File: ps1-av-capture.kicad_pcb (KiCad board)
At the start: 4 copper layers, 100 x 80 mm, 235 parts, among them J1 AV_MULTI_OUT, J2 USB3_B, J3 USB_C_AUDIO, J4 JTAG, J5 UART, SW1 RESET, U1 TVP7002PZP, U10 TLV75733PDBVR, U11 TLV75533PDBVR, U12 PCM2903CDBR, U2 CYUSB3014-BZXI, U3 24LC1025-I/SN, U4 24LC1025-I/SN, U5 TPS563201DDCR, U6 TPS563201DDCR, U7 TPS563201DDCR, U8 TLV75519PDBVR, U9 TLV75519PDBVR, X1 27MHz, Y1 19.2MHz, Y2 12MHz

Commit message: J1: JST PHD 2x7 latching header for a multi-AV pigtail, hand-soldered
Signals paired with grounds in each column, DNP in the JLC assembly.
Pigtail pinout and build steps in docs/design.md, hand-built items in docs/parts.md.
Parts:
- J1: value AV_MULTI_OUT -> AV_PIGTAIL; footprint Connector_PinHeader_2.54mm:PinHeader_1x13_P2.54mm_Vertical -> Connector_JST:JST_PHD_B14B-PHDSS_2x07_P2.00mm_Vertical
- moved J1 2.00 mm to (106.0, 112.0), turned to -90 degrees
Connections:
- J1 pad 1: VIN_G -> VIN_R
- J1 pad 11: AIN_R -> AIN_L
- J1 pad 13: GND -> AIN_R
- J1 pad 2: VIN_R -> GND
- J1 pad 3: unconnected-(J1-Pin_3-Pad3) -> VIN_G
- J1 pad 4: VIN_B -> GND
- J1 pad 5: GND -> VIN_B
- J1 pad 6: unconnected-(J1-Pin_6-Pad6) -> GND
- J1 pad 7: VIN_CVBS -> VIN_Y
- J1 pad 8: VIN_Y -> GND
- J1 pad 9: AIN_L -> VIN_CVBS

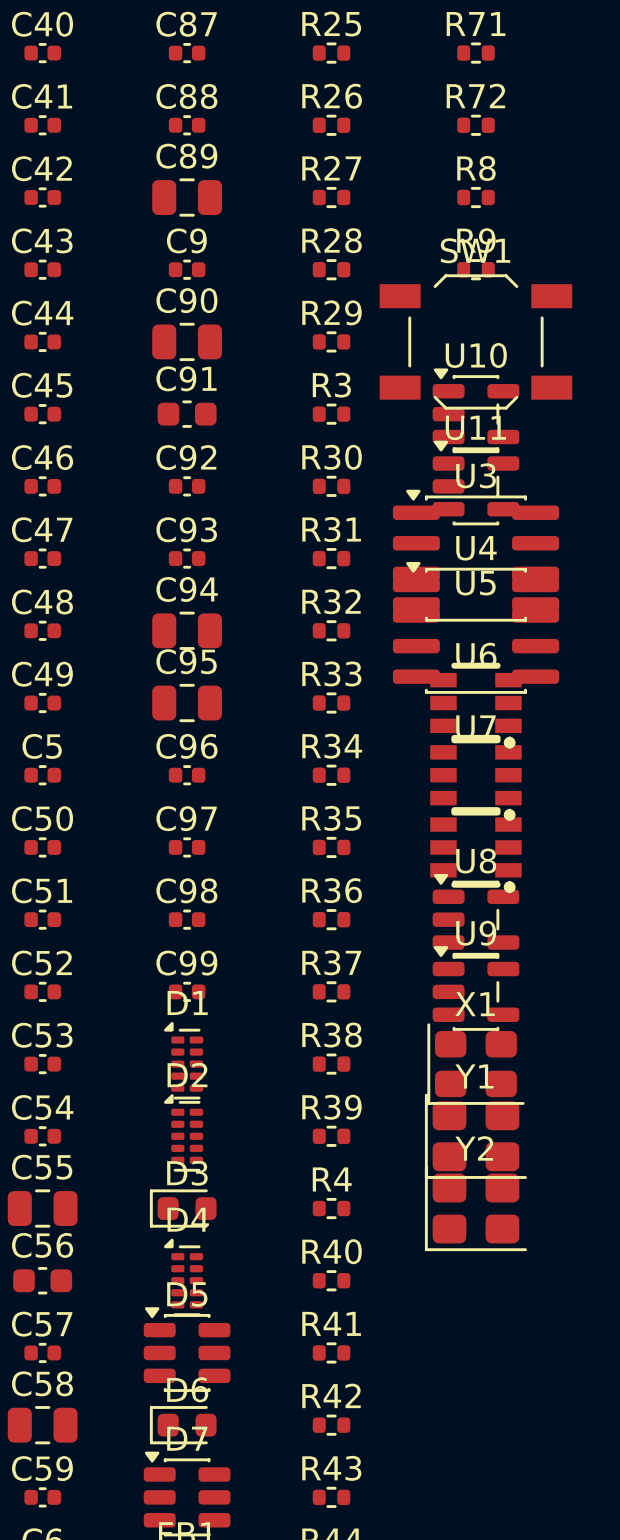
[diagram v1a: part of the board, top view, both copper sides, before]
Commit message: Status LED: common-anode RGB on FX3 GPIO50-52, firmware state map
XL-1615RGBC-RF (C965840) replaces the GPIO57 debug LED. Its LCSC pattern
numbers G and B the other way from the datasheet; fix_footprints.py renumbers
them and applies the datasheet's land pattern. GPIO budget in docs/design.md.
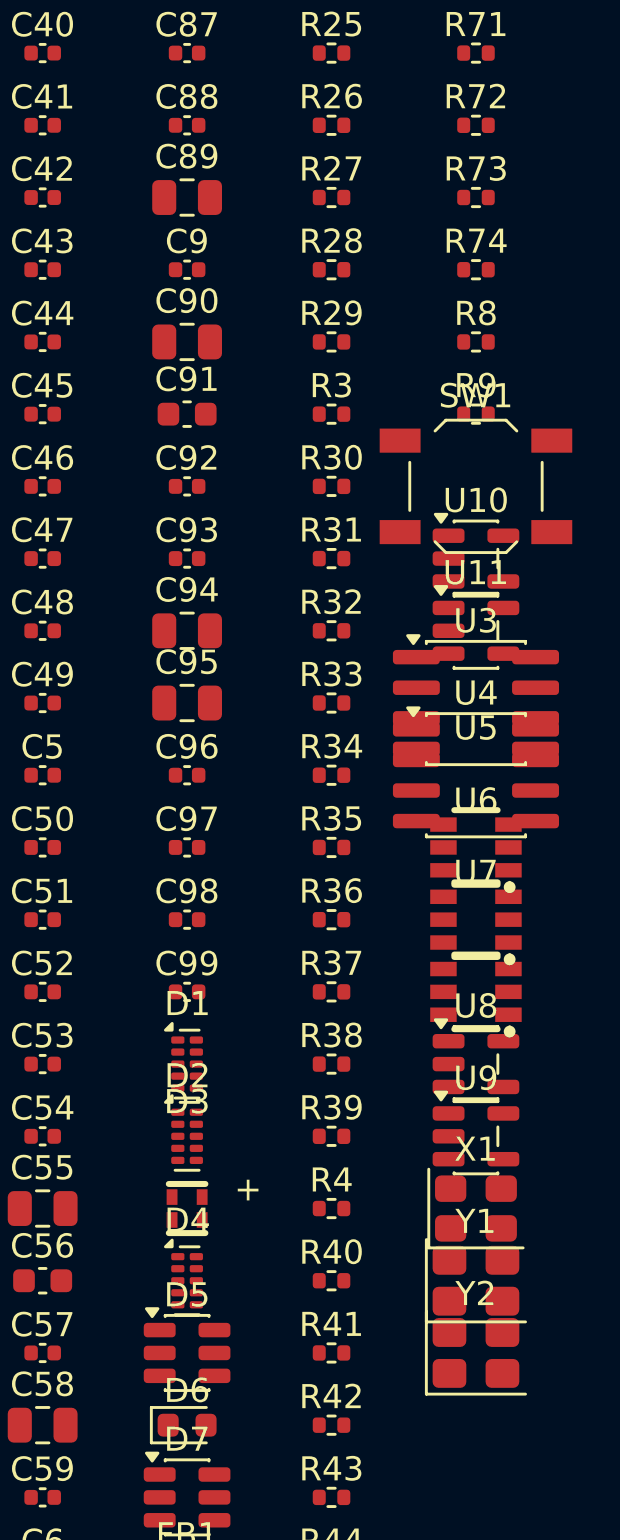
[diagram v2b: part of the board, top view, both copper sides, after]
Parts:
- added R73: 10k, Resistor_SMD:R_0402_1005Metric, F.Cu at (234.0, 118.0)
- added R74: 10k, Resistor_SMD:R_0402_1005Metric, F.Cu at (234.0, 121.0)
- D3: value GREEN -> XL-1615RGBC-RF; footprint LED_SMD:LED_0603_1608Metric -> ps1-av-capture:LED-ARRAY-SMD_4P-L1.6-W1.5-BR_XL-1615RGBC-RF
- R51: value 1k -> 470
- R52, R53: value 100k -> 100
- R54: value 33.2k 1% -> 100k
- R55, R58, R61: value 10k -> 100k
- R56: value 100k -> 33.2k 1%
- R57: value 22.6k 1% -> 10k
- R59: value 100k -> 22.6k 1%
- R60: value 5.76k 1% -> 10k
- R62: value 1k -> 5.76k 1%
- R63: value 5.1k -> 10k
- R64: value 5.1k -> 1k
- R65, R66: value 22 -> 5.1k
- R67: value 1.5k -> 22
- R68: value 1M -> 22
- R69: value 1M -> 1.5k
- R71, R72: value 10k -> 1M
- moved R8 6.00 mm to (234.0, 124.0)
- moved R9 6.00 mm to (234.0, 127.0)
- moved SW1 6.00 mm to (234.0, 130.0)
- moved U10 6.00 mm to (234.0, 133.0)
- moved U11 6.00 mm to (234.0, 136.0)
- moved U3 6.00 mm to (234.0, 139.0)
- moved U4 6.00 mm to (234.0, 142.0)
- moved U5 6.00 mm to (234.0, 145.0)
- moved U6 6.00 mm to (234.0, 148.0)
- moved U7 6.00 mm to (234.0, 151.0)
- moved U8 6.00 mm to (234.0, 154.0)
- moved U9 6.00 mm to (234.0, 157.0)
- moved X1 6.00 mm to (234.0, 160.0)
- moved Y1 6.00 mm to (234.0, 163.0)
- moved Y2 6.00 mm to (234.0, 166.0)
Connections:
- net FX3_LED_K renamed LED_R_K
- R51 pad 2: FX3_LED -> LED_R
- R52 pad 1: USB3_SHIELD -> LED_G_K
- R52 pad 2: GND -> LED_G
- R53 pad 1: VBUS -> LED_B_K
- R53 pad 2: EN_3V3 -> LED_B
- R54 pad 1: +3V3 -> USB3_SHIELD
- R54 pad 2: FB_3V3 -> GND
- R55 pad 1: FB_3V3 -> VBUS
- R55 pad 2: GND -> EN_3V3
- R56 pad 1: VBUS -> +3V3
- R56 pad 2: EN_2V5 -> FB_3V3
- R57 pad 1: +2V5 -> FB_3V3
- R57 pad 2: FB_2V5 -> GND
- R58 pad 1: FB_2V5 -> VBUS
- R58 pad 2: GND -> EN_2V5
- R59 pad 1: VBUS -> +2V5
- R59 pad 2: EN_1V2 -> FB_2V5
- R60 pad 1: +1V2 -> FB_2V5
- R60 pad 2: FB_1V2 -> GND
- R61 pad 1: FB_1V2 -> VBUS
- R61 pad 2: GND -> EN_1V2
- R62 pad 1: PWR_LED_K -> +1V2
- R62 pad 2: GND -> FB_1V2
- R63 pad 1: AUD_CC1 -> FB_1V2
- R64 pad 1: AUD_CC2 -> PWR_LED_K
- R65 pad 1: AUD_DP_C -> AUD_CC1
- R65 pad 2: AUD_DP -> GND
- R66 pad 1: AUD_DM_C -> AUD_CC2
- R66 pad 2: AUD_DM -> GND
- R67 pad 2: +3V3_AUD -> AUD_DP
- R68 pad 1: VBUS_AUD -> AUD_DM_C
- R68 pad 2: AUD_SEL1 -> AUD_DM
- R69 pad 1: AUD_SEL1 -> AUD_DP_C
- R69 pad 2: GND -> +3V3_AUD
- R70 pad 1: AUD_XI -> VBUS_AUD
- R70 pad 2: AUD_XO -> AUD_SEL1
- R71 pad 1: AIN_L_C -> AUD_SEL1
- R71 pad 2: AUD_VINL -> GND
- R72 pad 1: AIN_R_C -> AUD_XI
- R72 pad 2: AUD_VINR -> AUD_XO
- U2 pad C4: FX3_LED -> unconnected-(U2B-GPIO[57]-PadC4)
- U2 pad D1: unconnected-(U2B-GPIO[50]-PadD1) -> LED_R
- U2 pad D2: unconnected-(U2B-GPIO[51]-PadD2) -> LED_G
- U2 pad D3: unconnected-(U2B-GPIO[52]-PadD3) -> LED_B

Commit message: Layout: place every remaining part
Power block, LDOs and debug parts by hand; the rest next to the pad they
serve, pushed out until clear. Rail caps go to an IC on their own sheet,
spread over its rail pins; 75R terminations sit at J1. No courtyard overlaps.
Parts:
- moved R2 176.7 mm to (113.5, 107.6), turned to 90 degrees
- moved C80 167.3 mm to (115.9, 110.0), turned to 180 degrees
- moved C8 154.6 mm to (128.5, 113.6), turned to -90 degrees
- moved C33 153.4 mm to (122.5, 115.0), turned to 180 degrees
- moved R1 152.7 mm to (112.0, 108.1), turned to 90 degrees
- moved C32 148.1 mm to (126.0, 116.1), turned to 90 degrees
- moved R67 146.2 mm to (118.5, 153.2), turned to -90 degrees
- moved C31 144.7 mm to (127.5, 116.1), turned to 90 degrees
- moved R64 142.5 mm to (172.0, 110.0), turned to 180 degrees
- moved R15 141.6 mm to (118.0, 136.0), turned to -90 degrees
- moved R6 139.0 mm to (143.0, 116.0), turned to 90 degrees
- moved R14 138.4 mm to (119.5, 136.0), turned to -90 degrees
- moved R5 137.9 mm to (109.5, 122.5)
- moved R20 136.8 mm to (146.5, 136.0), turned to -90 degrees
- moved C36 136.6 mm to (142.9, 131.0)
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
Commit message: Layout: USB 3 corridor placed and routed, pairs length-matched
SS TX/RX on L1 from the FX3's row A through one flow-through TPD4E05U06 to
the receptacle; RX wired P-to-N as AN70707 p.22 allows. D+/D- through the
USBLC6, then L4. route_usb.py matches each pair by 45-degree bumps and prints
the lengths; L2 GND plane added.
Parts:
- moved C57 24.3 mm to (175.7, 160.5)
- moved R50 23.7 mm to (153.4, 164.0)
- moved C39 20.4 mm to (173.3, 165.2)
- moved C40 19.9 mm to (151.2, 160.5)
- moved Y1 18.4 mm to (172.5, 161.7)
- moved C56 18.0 mm to (171.2, 153.5)
- moved FB4 11.0 mm to (171.2, 157.0)
- moved R38 10.8 mm to (171.0, 150.7)
- moved C78 9.69 mm to (162.9, 156.6)
- moved R54 9.51 mm to (171.4, 170.7)
- moved C77 8.92 mm to (161.9, 156.6)
- moved D5 7.66 mm to (156.0, 157.5), turned to 180 degrees
- moved FB7 7.50 mm to (150.5, 157.0)
- moved C59 7.07 mm to (177.3, 161.5)
- moved C61 7.07 mm to (179.2, 161.5)
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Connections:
- D4 pad 1: USB3_TXP -> USB3_TXN
- D4 pad 10: unconnected-(D4-NC-Pad10) -> USB3_TXN
- D4 pad 2: USB3_TXN -> USB3_TXP
- D4 pad 6: unconnected-(D4-NC-Pad6) -> USB3_RXN
- D4 pad 7: unconnected-(D4-NC-Pad7) -> USB3_RXP
- D4 pad 9: unconnected-(D4-NC-Pad9) -> USB3_TXP
- J2 pad 8: USB3_RXN -> USB3_RXP
- J2 pad 9: USB3_RXP -> USB3_RXN
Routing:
- net USB3_DP: track 0.00 -> 27.1 mm, vias 0 -> 1
- net USB3_DM: track 0.00 -> 27.1 mm, vias 0 -> 1
- net USB3_RXN: track 0.00 -> 11.1 mm
- net USB3_RXP: track 0.00 -> 11.1 mm
- net USB3_TXP: track 0.00 -> 9.51 mm
- net USB3_TXN: track 0.00 -> 9.51 mm
- net USB3_TXP_C: track 0.00 -> 2.16 mm
- net USB3_TXN_C: track 0.00 -> 2.16 mm
- net GND: track 0.00 -> 1.53 mm, vias 0 -> 3
- added copper zone on In1.Cu, net GND

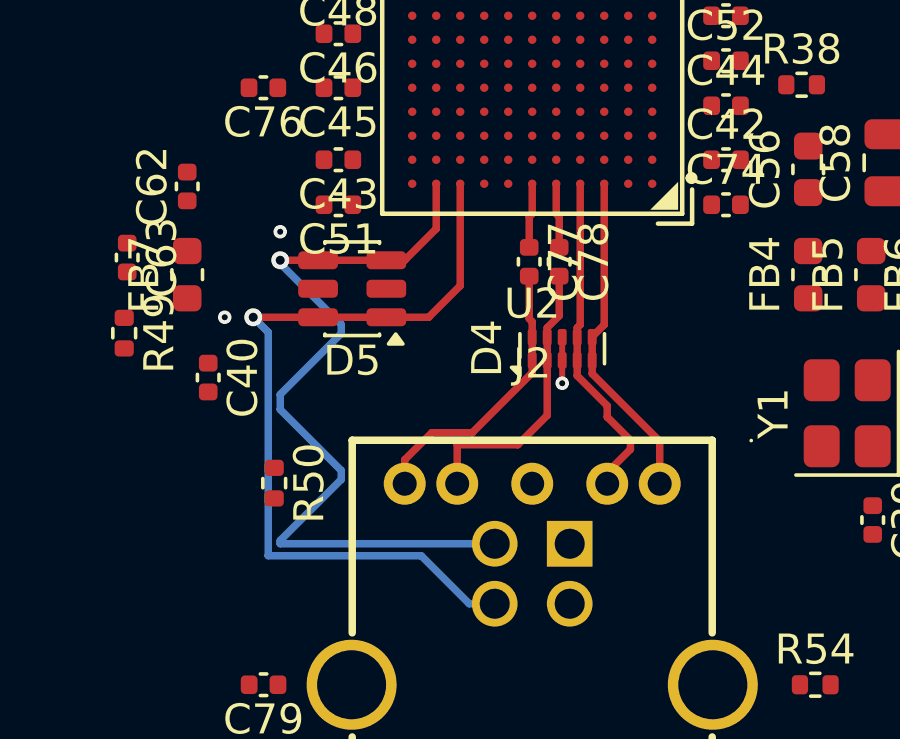
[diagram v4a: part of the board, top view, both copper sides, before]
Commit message: Layout: L3 supply planes, geometry checker, Freerouting export
L3 is +3V3 with a +1V2 island under the FX3 and its buck and GND under the
USB corridor, so the D+/D- run on L4 has a ground reference. check_geometry.py
from ps1-port-tap; the USB routing had 10 findings (90-degree corners, sub-width
jogs) and now has none. Hand routes are locked for the autorouter.
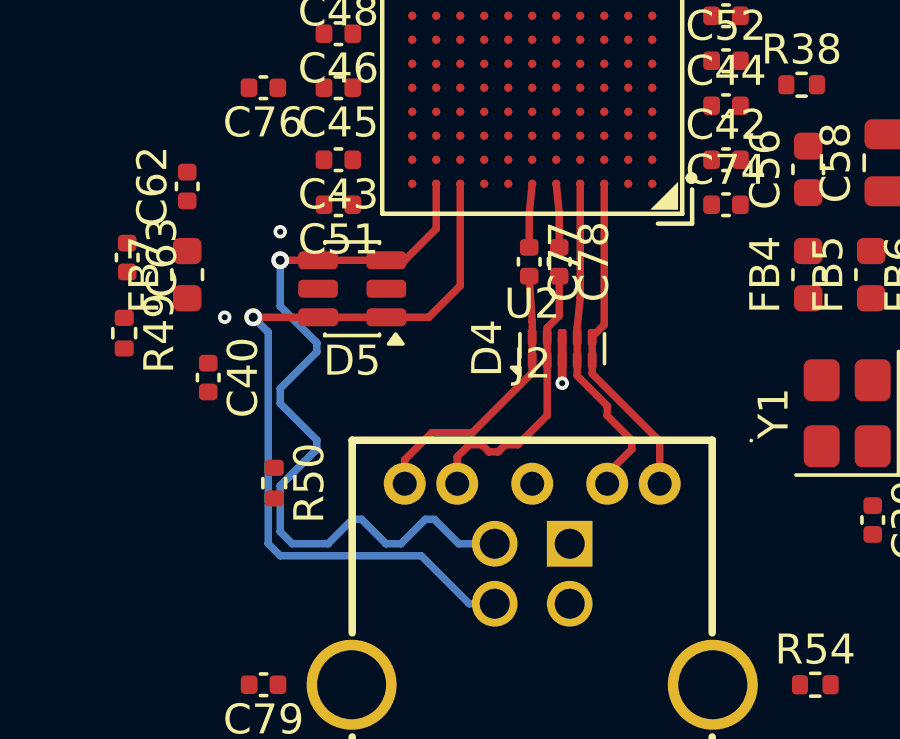
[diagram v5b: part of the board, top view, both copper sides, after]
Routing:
- added copper zone on In2.Cu, net +1V2
- added copper zone on In2.Cu, net +3V3
- added copper zone on In2.Cu, net GND

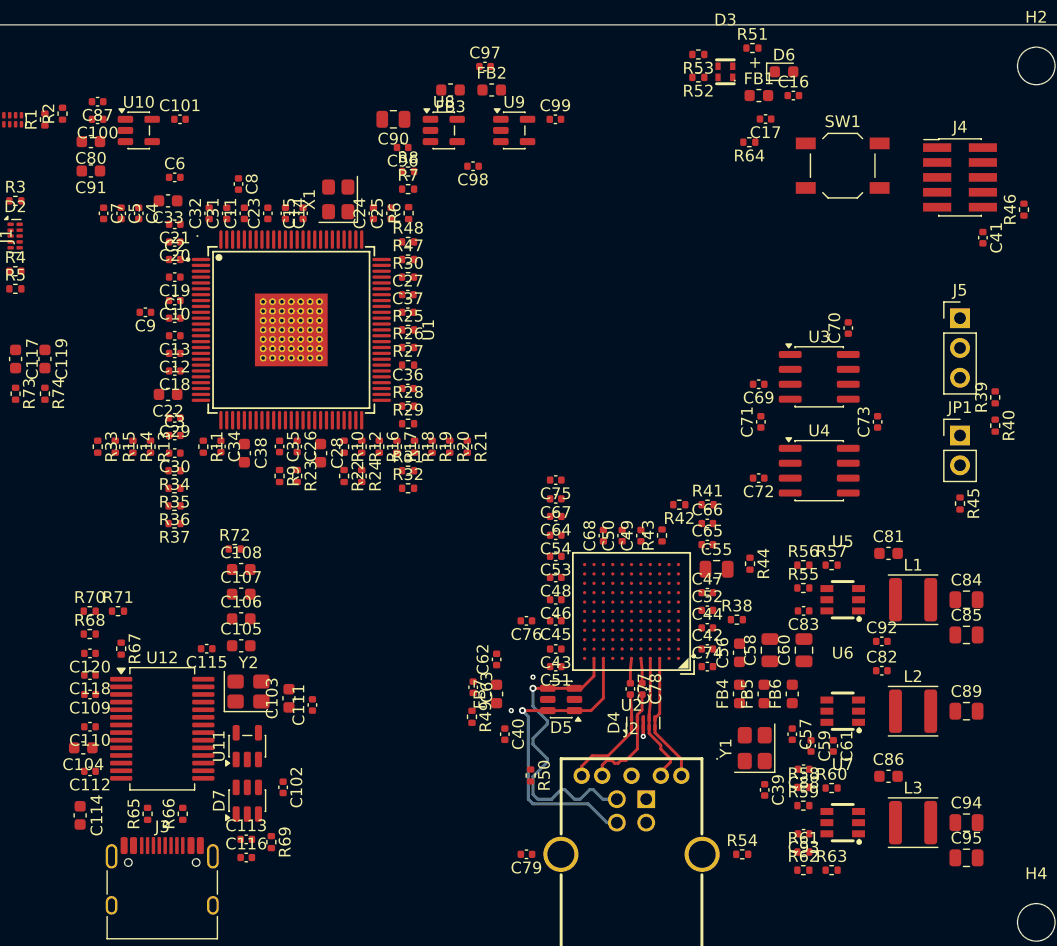
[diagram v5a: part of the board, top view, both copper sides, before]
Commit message: Layout: 0.45/0.2 vias and a 1.5 mm escape ring around U1/U2
Freerouting pass 2 with these: fanout escaped 489/802 SMD pins (pass 1: 499),
best routing 131 unrouted (pass 1: 164). Not converging; the next step is a
scripted plane fanout so the router only sees signal nets.
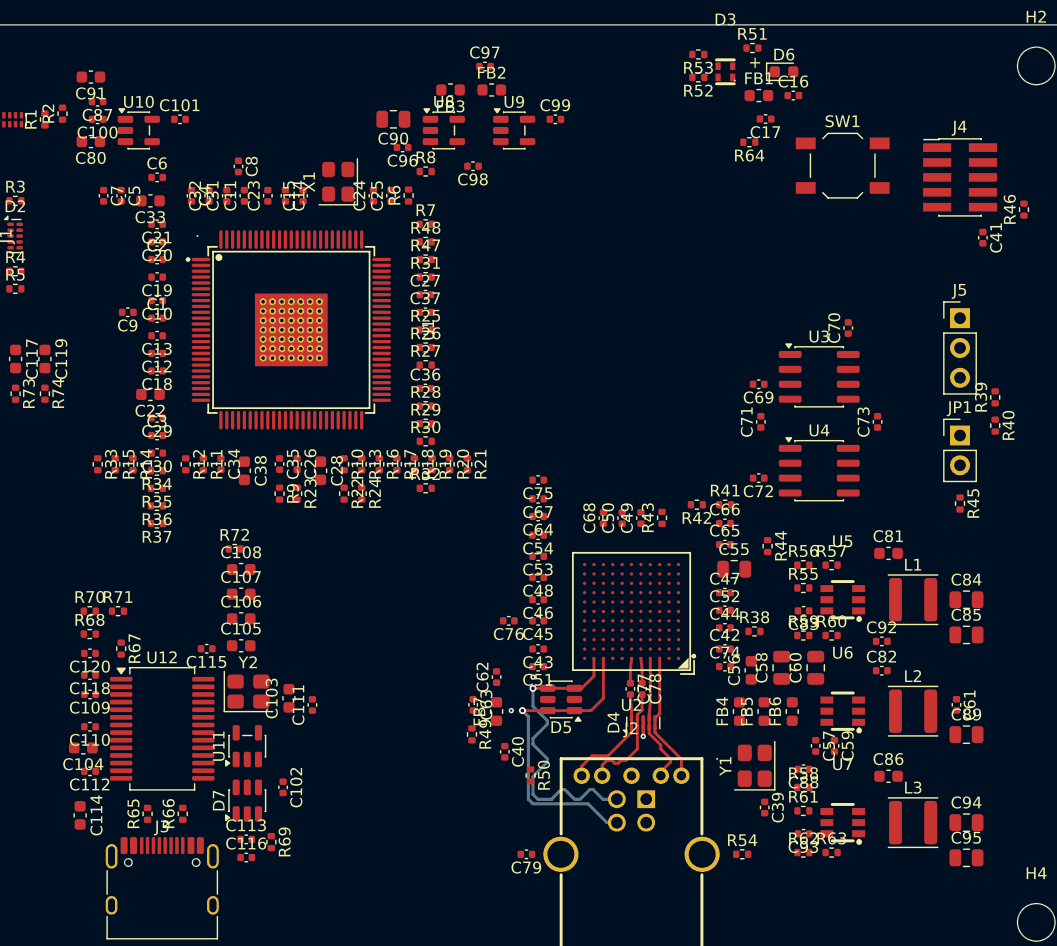
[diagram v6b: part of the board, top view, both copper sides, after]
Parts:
- moved R13 18.1 mm to (139.0, 137.5)
- moved R31 16.6 mm to (144.5, 121.5)
- moved R12 15.1 mm to (124.0, 137.5)
- moved R59 14.5 mm to (176.6, 152.1)
- moved R30 14.1 mm to (144.5, 135.5)
- moved R60 13.0 mm to (179.1, 152.1)
- moved C61 11.1 mm to (189.7, 158.0)
- moved C91 8.00 mm to (115.9, 104.5)
- moved C4 4.74 mm to (124.5, 114.6)
- moved R61 3.50 mm to (176.6, 167.0)
- moved R7 3.35 mm to (144.5, 117.0)
- moved C57 2.24 mm to (177.7, 161.5)
- moved R44 2.12 mm to (173.6, 144.4)
- moved C59 2.00 mm to (179.3, 161.5)
- moved C89 2.00 mm to (190.6, 160.5)
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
